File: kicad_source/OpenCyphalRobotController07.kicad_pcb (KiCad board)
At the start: 2 copper layers, 140 x 70 mm, 165 parts, among them J1 SM04B-SRSS-TB, J10 x, J11 PowerPole, J12 Conn_01x02, J13 Conn_01x02, J14 Conn_01x02, J2 RASPBERRYPI_PICO, J3 SM04B-SRSS-TB, J4 S3B-PH-SM4-TB, J5 BM04B-GHS-TBT, J6 BM04B-GHS-TBT, J7 x, J8 x, J9 x, Q1 2N7002, Q2 IPD90P03P4L- 04, SW1 PTS636 SM43 SMTR LFS, U1 24LC64-I/SN, U10 ADS1015IDGS, U11 OPA2374AIDCN, U12 INA226, U13 IFX91041EFJ, U14 ITS4200S-ME-P, U15 ITS4200S-ME-P, U16 BNO085, U2 MCP2515-I/SO, U3 SN65HVD232, U4 74xx08, U5 IFX007T, U6 IFX007T, U7 IFX007T, U8 IFX007T, U9 OPA2374AIDCN, Y1 RH100-16.000-16-3030-EXT-TR

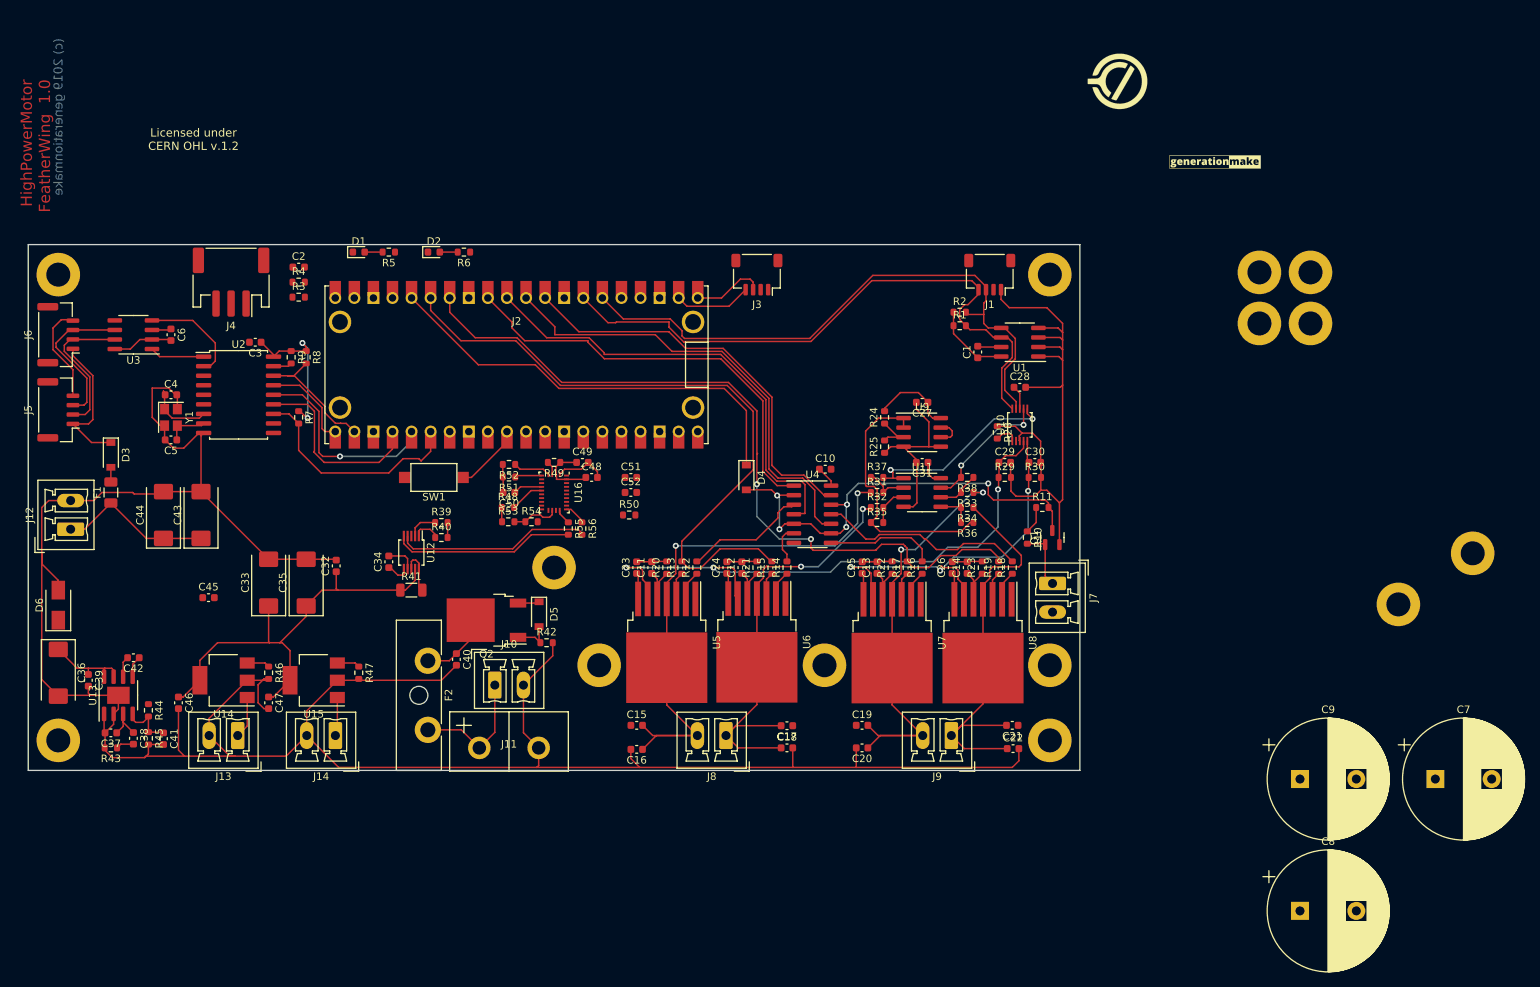
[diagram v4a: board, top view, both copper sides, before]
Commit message: updated layout
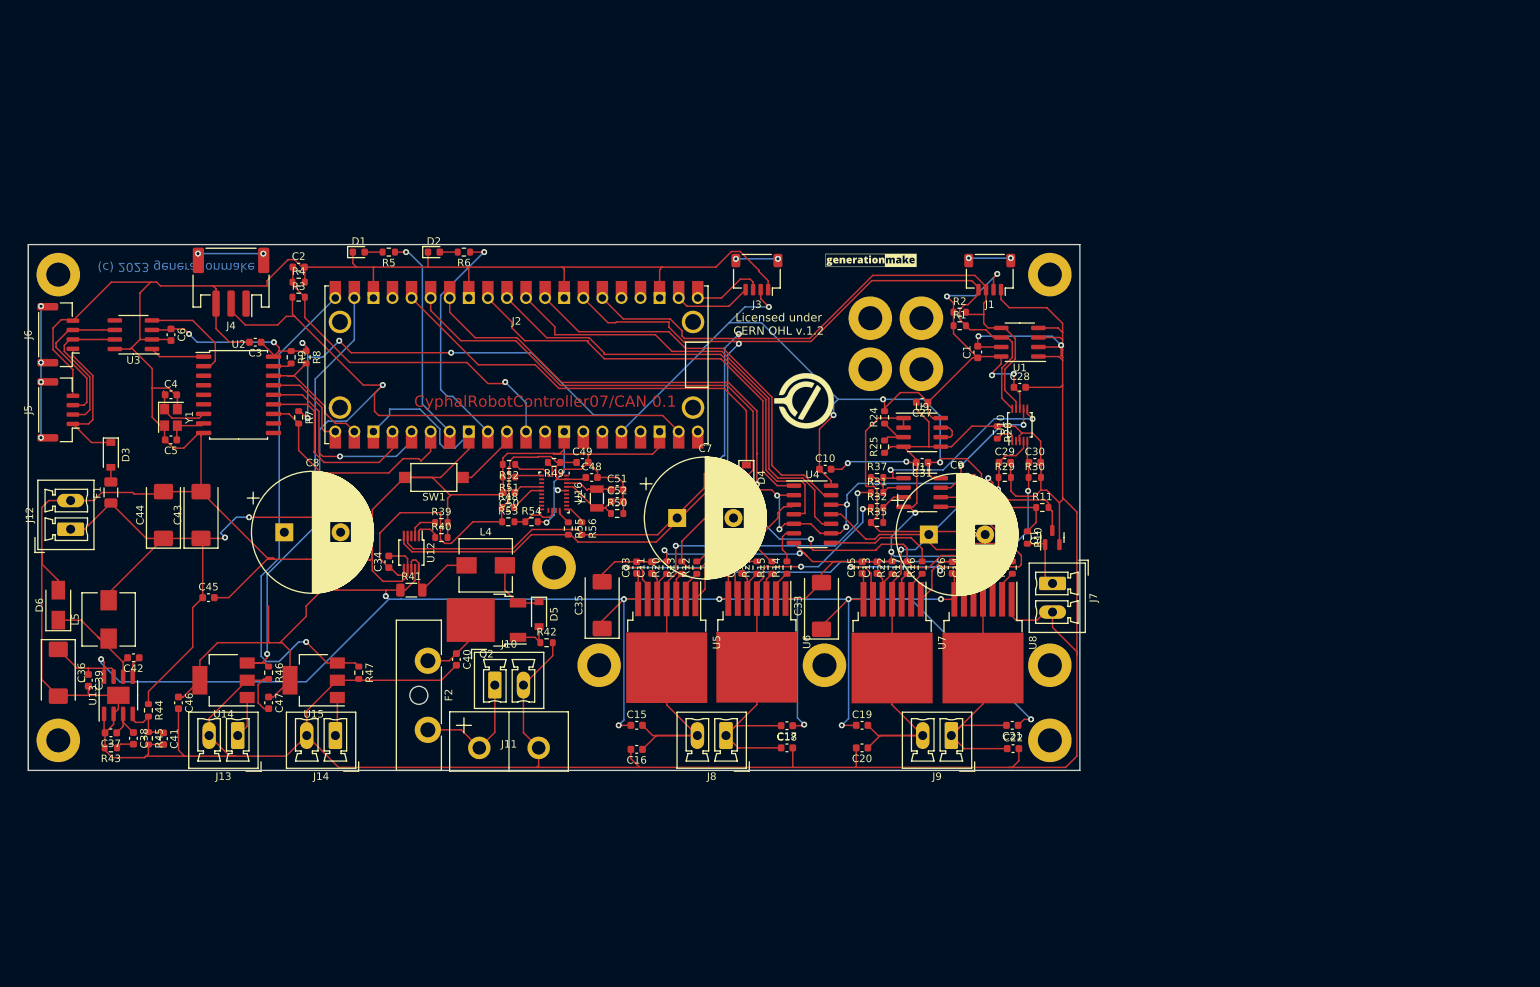
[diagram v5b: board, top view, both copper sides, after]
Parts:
- removed MECH10, MECH9: MHP_3.2_5.0, generationmake:MHP_3.2_5.8
- added L4: 744373580022, Inductor_SMD:L_Wuerth_HCI-7050, F.Cu at (111.9, 98.7)
- added L5: 74437346220, Inductor_SMD:L_Wuerth_HCI-7050, F.Cu at (61.7, 105.9)
- added Y2: DNI, Crystal:Crystal_SMD_3215-2Pin_3.2x1.5mm, F.Cu at (126.7, 89.8)
- moved C8 144.3 mm to (85.1, 94.3)
- moved C7 106.7 mm to (137.4, 92.4)
- moved C33 73.7 mm to (156.6, 104.1)
- moved L3 59.6 mm to (154.3, 76.8)
- moved C9 59.2 mm to (170.9, 94.6)
- moved MECH11 52.2 mm to (163.1, 65.8)
- moved MECH12 52.2 mm to (163.1, 72.6)
- moved MECH13 52.2 mm to (169.9, 65.8)
- moved MECH14 52.2 mm to (169.9, 72.6)
- moved L1 47.6 mm to (163.2, 60.7)
- moved L2 43.7 mm to (162.7, 63.7)
- moved C35 39.5 mm to (127.4, 104.0)
- moved C51 2.43 mm to (129.4, 88.6)
- moved C52 2.18 mm to (129.4, 90.2)
- moved R50 1.61 mm to (129.4, 91.8)
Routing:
- net GND: track 504.7 -> 969.9 mm, vias 0 -> 12
- net +BATT: track 84.1 -> 307.6 mm, vias 0 -> 10
- net +3.3V: track 57.7 -> 251.5 mm, vias 2 -> 14
- net I2C_SCL: track 107.5 -> 300.3 mm, vias 0 -> 4
- net +5V: track 20.8 -> 174.3 mm, vias 0 -> 4
- net I2C_SDA: track 106.9 -> 0.00 mm
- net OUTPUT1: track 3.05 -> 67.5 mm, vias 0 -> 1
- net OUT3: track 58.1 -> 121.4 mm
- net OUTPUT0: track 3.05 -> 58.7 mm, vias 0 -> 1
- net /+BATT_MEAS: track 0.00 -> 45.6 mm, vias 0 -> 1
- net +3V3: track 13.8 -> 55.2 mm
- net /Measurement/VREF: track 35.4 -> 0.00 mm
- net /LED3: track 0.00 -> 31.2 mm, vias 0 -> 1
- net /LED2: track 0.00 -> 27.9 mm, vias 0 -> 1
- net /MotorDriver/PWM4_U: track 27.9 -> 0.00 mm
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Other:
- board text added: "(c) 2023 generationmake"
- board text added: "CyphalRobotController07/CAN 0.1"
- board text removed: "(c) 2019 generationmake"
- board text removed: "HighPowerMotor FeatherWing 1.0"
- board text removed: "for Adafruit Feather"
